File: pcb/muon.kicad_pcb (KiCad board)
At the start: 2 copper layers, 57 x 50 mm, 51 parts, among them J1 Debug Pins, J2 USB_C_Receptacle_USB2.0, SW1 SW_Push, SW2 SW_Push, SW3 Reset, U1 SRV05-4, U2 AP2112, U3 RP2040, U4 W25Q80DVSSIG, Y1 Crystal_GND24_Small

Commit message: minor fixes and shuffle
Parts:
- D3: value PWR LED -> STATUS LED
- moved R9 21.9 mm to (144.7, 61.0), turned to 180 degrees
- moved D3 17.9 mm to (146.7, 61.0), turned to 180 degrees
- moved U4 13.6 mm to (165.8, 66.0)
- moved C8 10.6 mm to (170.0, 75.2), turned to -90 degrees
- moved R2 10.0 mm to (134.2, 76.0)
- moved LED1 10.0 mm to (141.5, 76.8)
- moved LED2 10.0 mm to (165.2, 76.8)
- moved C6 9.76 mm to (145.8, 76.0)
- moved C3 4.50 mm to (166.2, 60.0)
- moved F1 4.50 mm to (160.1, 59.2)
- moved U2 4.50 mm to (163.6, 59.2)
- moved C2 4.50 mm to (160.6, 60.6)
- moved C7 3.76 mm to (139.8, 96.0)
- moved C21 2.43 mm to (130.0, 65.8)
- moved D2 2.02 mm to (171.0, 92.2)
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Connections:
- R9 pad 2: +3V3 -> /STATUS
- U3 pad 14: unconnected-(U3-Pad14) -> /STATUS
- U3 pad 2: /SW1 -> unconnected-(U3-Pad2)
- U3 pad 3: /SW2 -> unconnected-(U3-Pad3)
- U3 pad 34: unconnected-(U3-Pad34) -> /UNDERGLOW
- U3 pad 39: unconnected-(U3-Pad39) -> /SW2
- U3 pad 40: /UNDERGLOW -> /SW1
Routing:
- net /5V_LED: track 127.1 -> 141.1 mm
- net /SW2: track 39.1 -> 52.5 mm
- net /QSPI_CS: track 10.0 -> 22.9 mm
- net /QSPI_CLK: track 20.8 -> 32.8 mm
- net /QSPI_1: track 11.2 -> 23.2 mm
- net /SW1: track 32.7 -> 21.4 mm
- net /QSPI_2: track 12.2 -> 23.4 mm
- net /QSPI_0: track 19.7 -> 30.1 mm
- net /QSPI_3: track 22.5 -> 32.8 mm
- net /KEYGLOW: track 21.7 -> 12.0 mm
- net +3V3: track 97.2 -> 100.8 mm
- net /~{RESET}: track 28.8 -> 30.3 mm
- net /STATUS: track 0.00 -> 1.42 mm
- net /UNDERGLOW: track 33.1 -> 34.4 mm
- net Net-(D1-Pad2): track 34.1 -> 32.9 mm
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
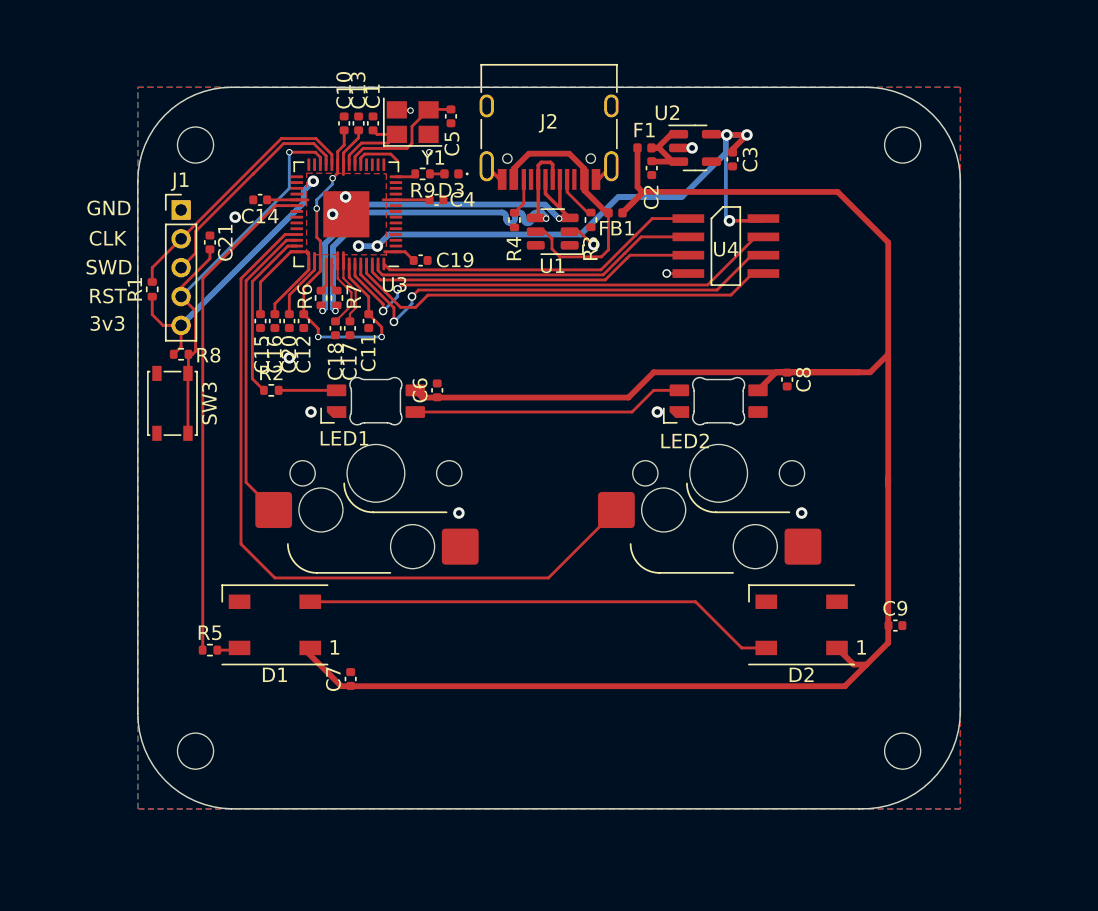
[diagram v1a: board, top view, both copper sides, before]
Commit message: all but 3 traces connected
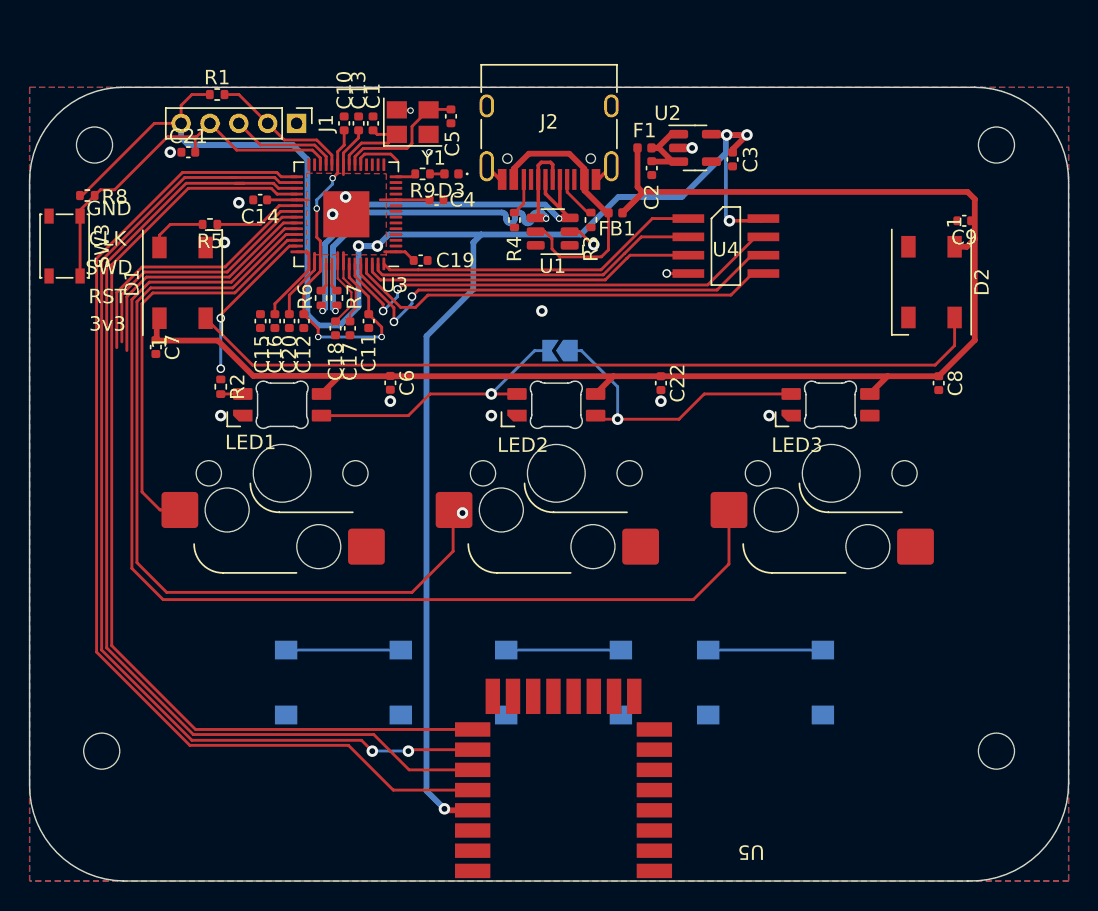
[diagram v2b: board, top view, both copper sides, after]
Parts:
- added C22: 100nF, Capacitor_SMD:C_0402_1005Metric, F.Cu at (161.2, 75.5)
- added JP1: Jumper_2_Open, Jumper:SolderJumper-2_P1.3mm_Open_TrianglePad1.0x1.5mm, B.Cu at (154.2, 73.2)
- added LED3: SK6812MINI-E, marbastlib-various:LED_6028R, F.Cu at (173.0, 77.0)
- added SW4: DTSM-66R-V-T/R, Button_Switch_SMD:SW_Push_1P1T_NO_6x6mm_H9.5mm, B.Cu at (139.2, 96.2)
- added SW5: DTSM-66R-V-T/R, Button_Switch_SMD:SW_Push_1P1T_NO_6x6mm_H9.5mm, B.Cu at (154.5, 96.2)
- added SW6: DTSM-66R-V-T/R, Button_Switch_SMD:SW_Push_1P1T_NO_6x6mm_H9.5mm, B.Cu at (168.5, 96.2)
- added SW7: Kaliah Hotswap, Keyswitch:SW_Hotswap_Kailh_MX_1.00u, B.Cu at (173.1, 81.8)
- added U5: DWM3000, qorvo:DWM3000, F.Cu at (161.0, 97.0)
- SW1, SW2: value SW_Push -> Kaliah Hotswap; footprint Keyswitch:SW_Hotswap_Kailh_MX_1.25u -> Keyswitch:SW_Hotswap_Kailh_MX_1.00u
- moved R5 29.5 mm to (130.0, 64.5), turned to 180 degrees
- moved C9 28.5 mm to (182.3, 64.2), turned to 180 degrees
- moved C7 26.7 mm to (126.2, 73.0), turned to -90 degrees
- moved D2 25.4 mm to (180.0, 68.5), turned to -90 degrees
- moved D1 24.5 mm to (128.1, 68.5), turned to 90 degrees
- moved R1 14.2 mm to (130.5, 55.5), turned to 0 degrees
- moved SW3 13.2 mm to (119.9, 66.0)
- moved R8 12.8 mm to (121.5, 62.5)
- moved LED2 11.3 mm to (154.0, 77.0)
- moved SW2 11.2 mm to (154.0, 81.8)
- moved C8 10.5 mm to (180.5, 75.5)
- moved J1 10.0 mm to (136.0, 57.5), turned to -90 degrees
- moved REF** 7.00 mm to (122.0, 59.0)
- moved LED1 6.50 mm to (135.0, 77.0)
- moved REF** 6.50 mm to (122.5, 101.0)
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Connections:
- LED2 pad 2: unconnected-(LED2-Pad2) -> Net-(LED2-Pad2)
- U3 pad 29: unconnected-(U3-Pad29) -> /D_CLK
- U3 pad 30: unconnected-(U3-Pad30) -> /D_MOSI
- U3 pad 31: unconnected-(U3-Pad31) -> /D_MISO
- U3 pad 32: unconnected-(U3-Pad32) -> /D_CS
- U3 pad 35: unconnected-(U3-Pad35) -> /FN1
- U3 pad 36: unconnected-(U3-Pad36) -> /FN2
- U3 pad 37: unconnected-(U3-Pad37) -> /FN3
- U3 pad 38: unconnected-(U3-Pad38) -> /SW3
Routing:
- net /SW3: track 0.00 -> 79.1 mm
- net /D_CLK: track 0.00 -> 73.8 mm
- net /D_MOSI: track 0.00 -> 71.9 mm, vias 0 -> 2
- net /D_MISO: track 0.00 -> 71.7 mm
- net /D_CS: track 0.00 -> 69.0 mm
- net +3V3: track 100.8 -> 162.0 mm
- net /5V_LED: track 141.1 -> 107.5 mm
- net /UNDERGLOW: track 34.4 -> 6.04 mm
- net /FN1: track 0.00 -> 26.6 mm
- net /FN2: track 0.00 -> 25.6 mm
- net /FN3: track 0.00 -> 25.6 mm
- net Net-(D1-Pad2): track 32.9 -> 55.8 mm
- net Net-(LED2-Pad2): track 0.00 -> 20.9 mm, vias 0 -> 1
- net /SWCLK: track 18.0 -> 9.53 mm
- net /SWD: track 15.5 -> 7.57 mm
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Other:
- board size 57 x 50 mm -> 72 x 55 mm

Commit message: pre v0.3
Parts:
- moved SW3 34.8 mm to (129.5, 99.5), turned to 0 degrees
- moved R8 6.36 mm to (126.0, 58.0), turned to 90 degrees
- moved SW4 4.75 mm to (139.2, 101.0)
- moved SW5 4.75 mm to (154.5, 101.0)
- moved SW6 4.75 mm to (168.5, 101.0)
- moved REF** 4.00 mm to (122.5, 105.0)
- moved REF** 4.00 mm to (184.5, 105.0)
- moved REF** 1.12 mm to (122.5, 60.0)
- moved REF** 0.71 mm to (185.0, 59.5)
- moved U5 0.49 mm to (161.0, 96.5)
- moved JP1 0.25 mm to (154.0, 73.2)
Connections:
- U5 pad 21: +3V3 -> GND
- U5 pad 5: unconnected-(U5-Pad5) -> +3V3
- U5 pad 6: unconnected-(U5-Pad6) -> +3V3
- U5 pad 7: unconnected-(U5-Pad7) -> +3V3
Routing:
- net /FN3: track 25.6 -> 89.9 mm, vias 0 -> 1
- net /FN2: track 25.6 -> 76.8 mm, vias 0 -> 1
- net /~{RESET}: track 26.9 -> 68.7 mm
- net /FN1: track 26.6 -> 62.4 mm, vias 0 -> 1
- net +3V3: track 162.0 -> 176.1 mm
- net /D_MISO: track 71.7 -> 68.7 mm
- net /D_MOSI: track 71.9 -> 69.2 mm
- net /D_CS: track 69.0 -> 66.6 mm
- net /D_CLK: track 73.8 -> 71.4 mm
- net /KEYGLOW: track 11.0 -> 11.7 mm
- net GND: track 10.7 -> 11.3 mm, vias 17 -> 16
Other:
- outline, holes or cut-outs redrawn

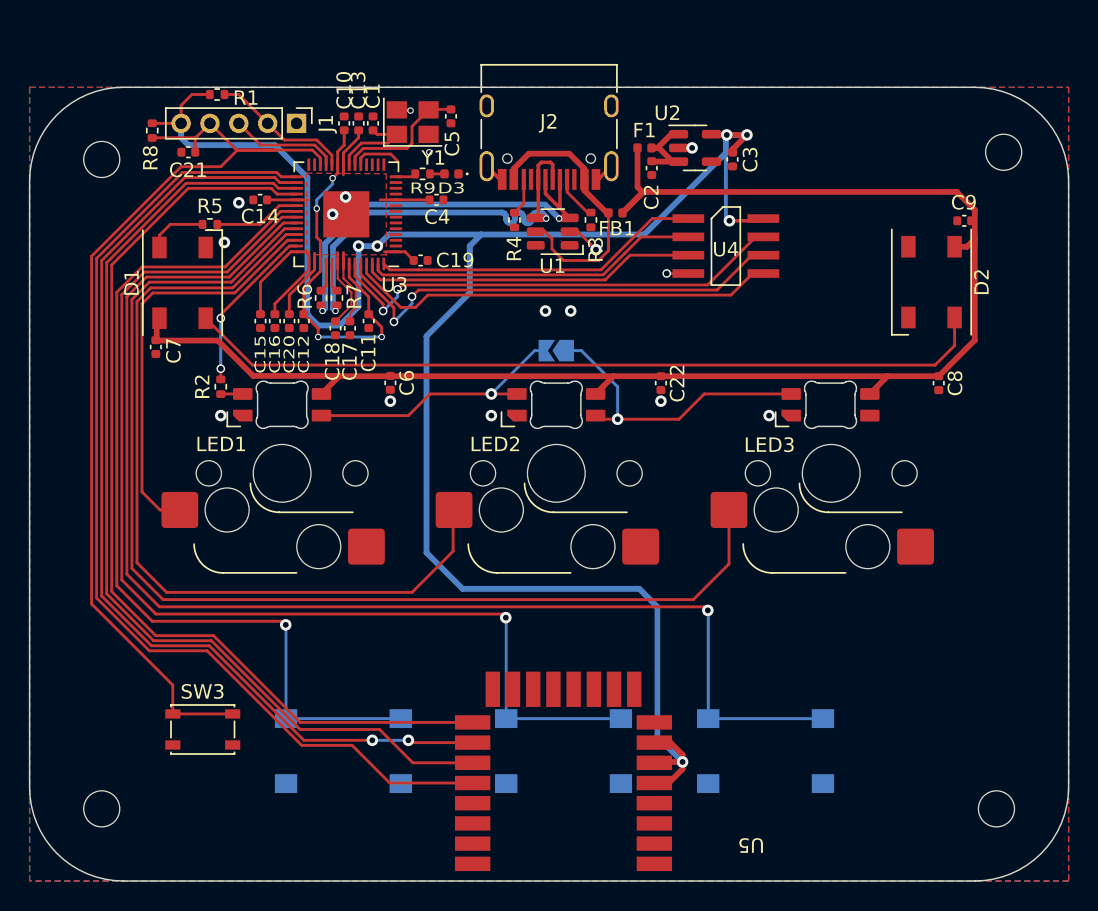
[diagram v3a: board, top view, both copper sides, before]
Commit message: remove wireless, change LDO to more avaliable one, decouple USB shield
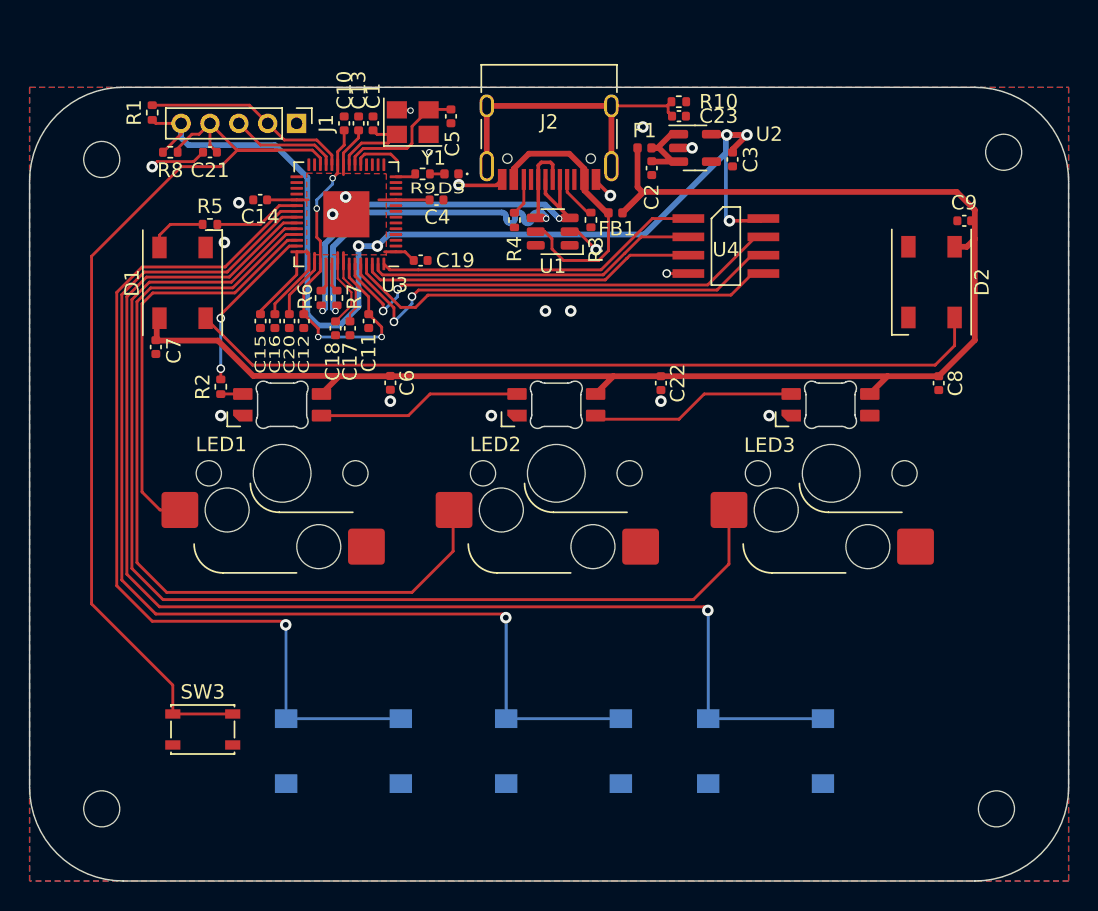
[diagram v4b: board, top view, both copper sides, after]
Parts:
- removed JP1: Jumper_2_Open, Jumper:SolderJumper-2_P1.3mm_Open_TrianglePad1.0x1.5mm
- removed U5: DWM3000, qorvo:DWM3000
- added C23: 100nF, Capacitor_SMD:C_0402_1005Metric, F.Cu at (162.5, 57.0)
- added R10: 1M, Resistor_SMD:R_0402_1005Metric, F.Cu at (162.5, 56.0)
- C2, C3: value 10uF -> 1uF
- R9: value 1k -> 10k
- SW1, SW2, SW7: value Kaliah Hotswap -> Kailh Hotswap
- U2: value AP2112 -> TLV75533PDBVR
- moved R1 4.67 mm to (126.0, 56.8), turned to 90 degrees
- moved R8 1.95 mm to (127.2, 59.5), turned to 180 degrees
- moved C21 1.50 mm to (130.0, 59.5)
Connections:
- J2 pad S1: GND -> Net-(J2-PadS1)
- U3 pad 29: /D_CLK -> unconnected-(U3-Pad29)
- U3 pad 30: /D_MOSI -> unconnected-(U3-Pad30)
- U3 pad 31: /D_MISO -> unconnected-(U3-Pad31)
- U3 pad 32: /D_CS -> unconnected-(U3-Pad32)
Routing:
- net /D_CLK: track 71.4 -> 0.00 mm
- net /D_MOSI: track 69.2 -> 0.00 mm, vias 2 -> 0
- net /D_MISO: track 68.7 -> 0.00 mm
- net /D_CS: track 66.6 -> 0.00 mm
- net +3V3: track 176.1 -> 115.2 mm, vias 6 -> 5
- net Net-(J2-PadS1): track 0.00 -> 22.5 mm
- net Net-(LED2-Pad2): track 21.2 -> 14.4 mm, vias 1 -> 0
- net GND: track 11.3 -> 16.9 mm, vias 16 -> 20
- net /SWCLK: track 9.53 -> 14.5 mm
- net Net-(LED1-Pad2): track 19.2 -> 14.2 mm, vias 1 -> 0

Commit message: revised v0.4, hybrid hotswap socket, fix off-center switches (off by .5mm)
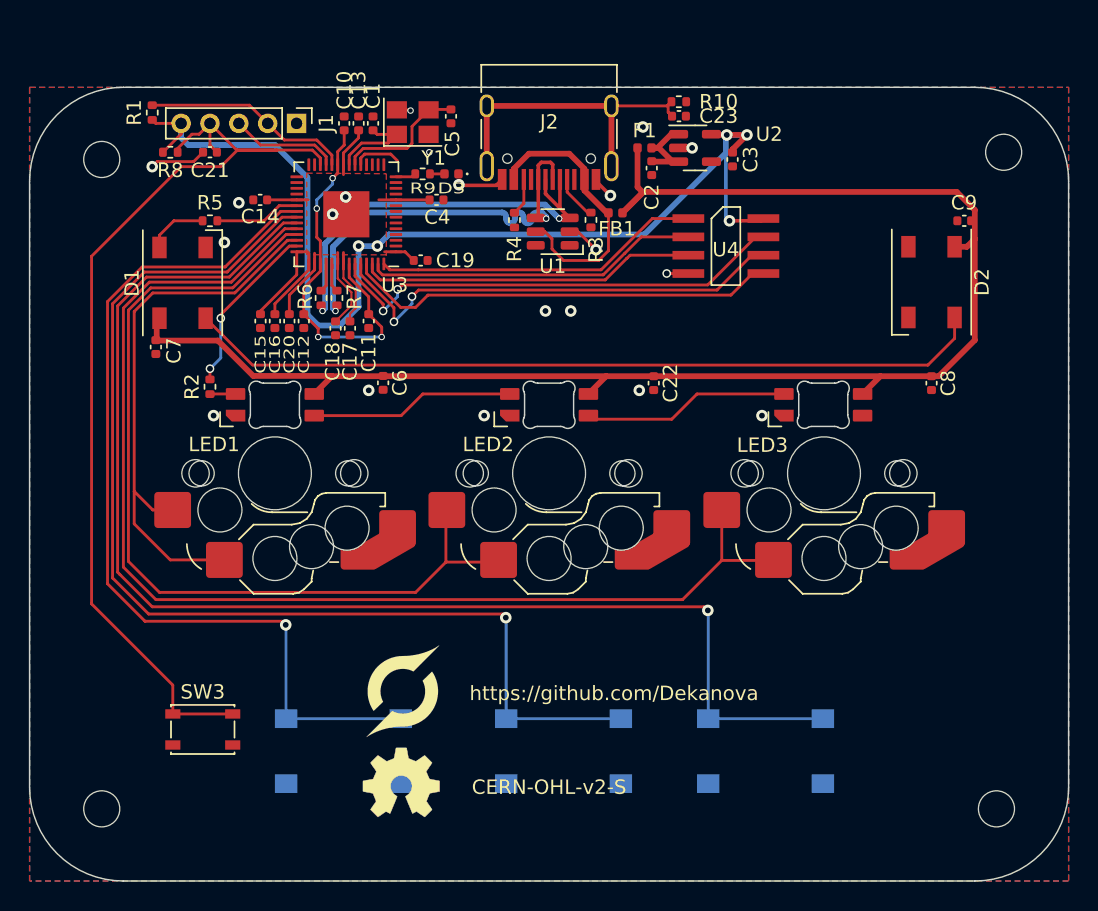
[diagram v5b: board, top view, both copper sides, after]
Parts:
- added kibuzzard-63119D27: G***, kibuzzard-63119D27, B.Cu at (178.8, 59.5)
- added kibuzzard-63119D36: G***, kibuzzard-63119D36, B.Cu at (173.0, 59.5)
- SW1, SW2, SW7: footprint Keyswitch:SW_Hotswap_Kailh_MX_1.00u -> local-hybrid:SW_Hotswap_Hybrid_1.00u
- moved R2 0.75 mm to (130.0, 75.8)
- moved C22 0.50 mm to (160.8, 75.5)
- moved C6 0.50 mm to (142.0, 75.5)
- moved C8 0.50 mm to (180.0, 75.5)
- moved LED1 0.50 mm to (134.5, 77.0)
- moved LED2 0.50 mm to (153.5, 77.0)
- moved LED3 0.50 mm to (172.5, 77.0)
- moved SW1 0.50 mm to (134.5, 81.8)
- moved SW2 0.50 mm to (153.5, 81.8)
- moved SW7 0.50 mm to (172.6, 81.8)
- moved R5 0.25 mm to (130.0, 64.2)
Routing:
- net /SW1: track 28.7 -> 38.5 mm
- net /SW2: track 57.9 -> 62.3 mm
- net /SW3: track 79.1 -> 82.9 mm
- net /FN3: track 89.9 -> 90.7 mm
- net /FN1: track 62.4 -> 63.2 mm
- net /FN2: track 76.8 -> 77.6 mm
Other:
- board text added: "CERN-OHL-v2-S"
- board text added: "https://github.com/Dekanova"

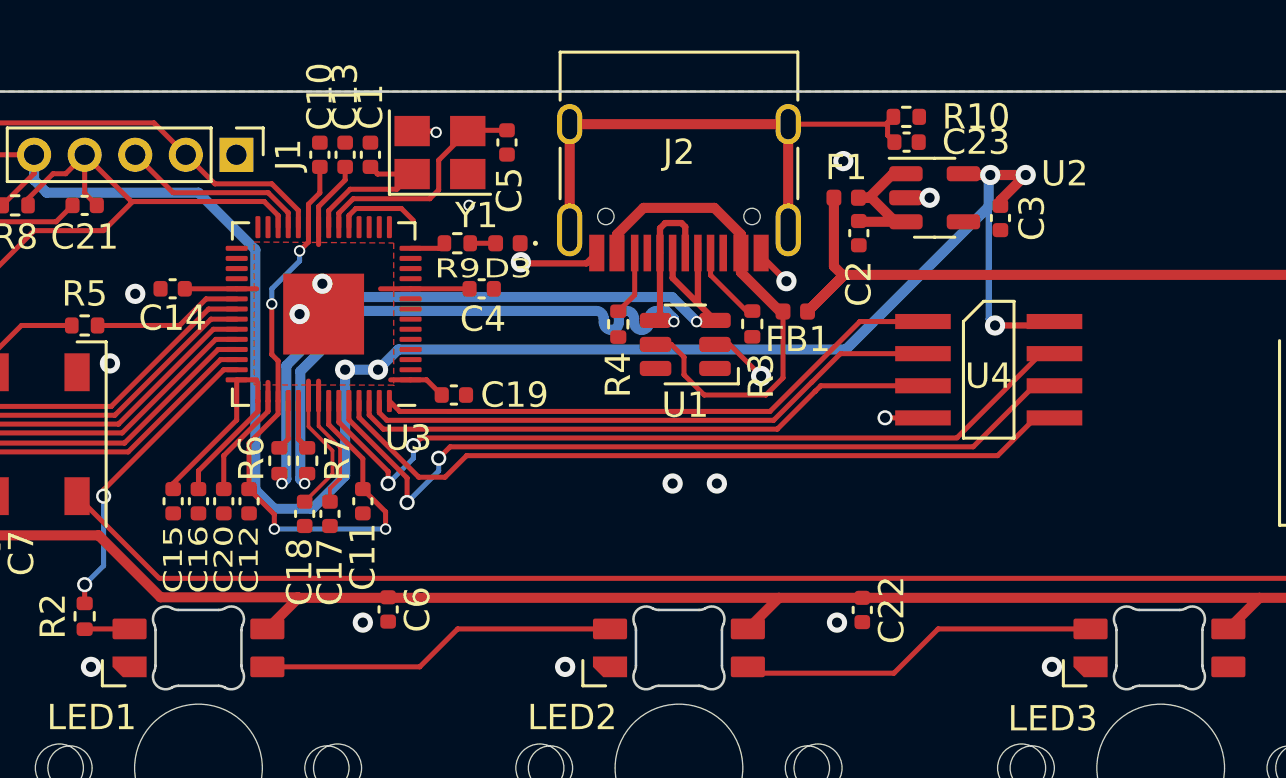
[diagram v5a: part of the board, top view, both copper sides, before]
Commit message: Change USB port to be on opposite side
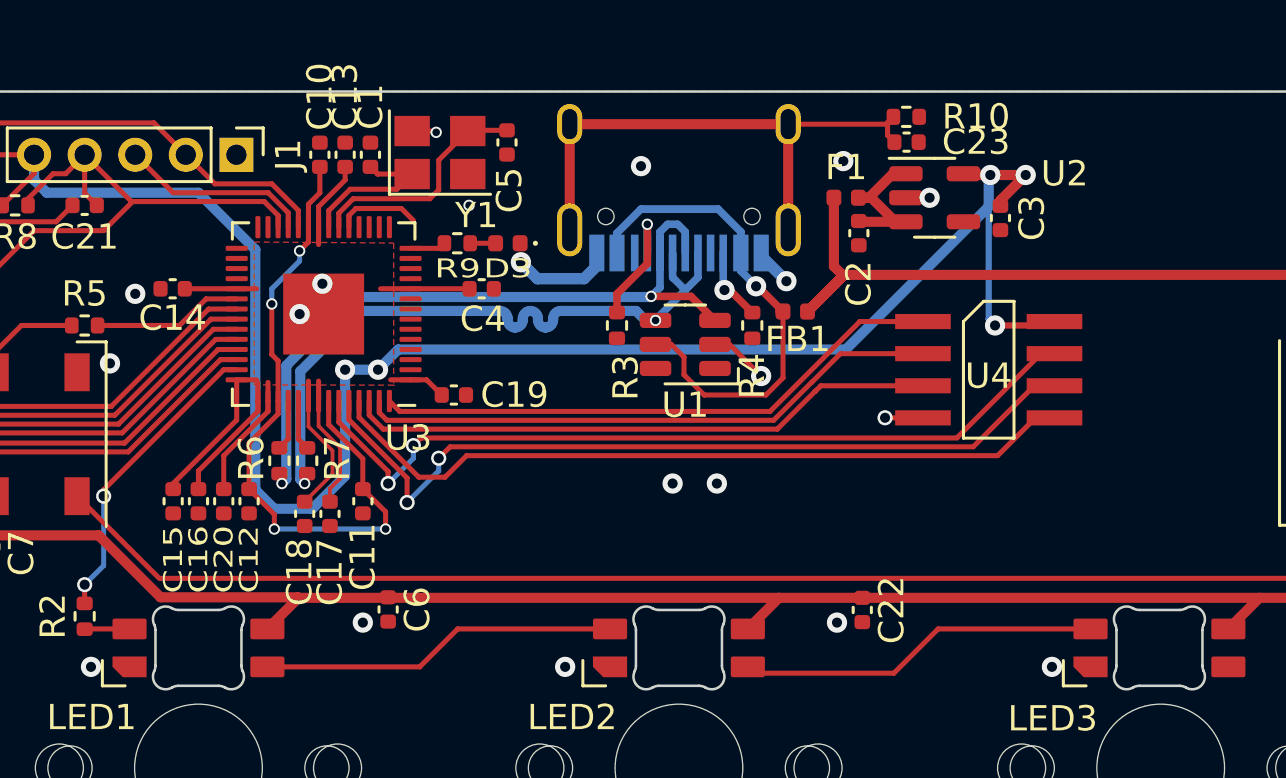
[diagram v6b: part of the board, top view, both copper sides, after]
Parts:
- J2: moved to B.Cu
- moved R3 5.35 mm to (151.1, 64.2)
- moved R4 5.30 mm to (156.4, 64.2)
- turned J2 to 0 degrees
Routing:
- net Net-(J2-PadA5): track 3.11 -> 5.12 mm, vias 0 -> 1
- net /D+: track 28.3 -> 26.3 mm
- net GND: track 16.9 -> 17.7 mm, vias 20 -> 21
- net Net-(J2-PadB5): track 2.57 -> 2.95 mm, vias 0 -> 1
- net /VBUS_: track 19.5 -> 19.6 mm, vias 0 -> 1
